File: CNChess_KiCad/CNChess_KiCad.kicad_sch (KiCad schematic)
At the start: 30 parts, among them J1 Servomotor, J2 Barrel_Jack, J3 Motor1, J4 Motor2, J5 Fan, SW1 Limit switch 1, SW2 Limit switch 2, SW3 On/off switch, U1 ESP32C3

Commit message: update kicad schematic
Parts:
- removed C3, C4: 1000uF, symbol Device:C
- removed R3: 10k, symbol Device:R_US
- removed R4: 47k, symbol Device:R_US
- removed TP2: TP3V3, symbol Connector:TestPoint
- added C3, C4: 1000uF, Capacitor_THT:CP_Radial_D8.0mm_P3.50mm, symbol Device:C_Polarized_US
- added D3, D4: LED, Connector_JST:JST_XH_B2B-XH-A_1x02_P2.50mm_Vertical, symbol Device:LED
- added R7: 270, Resistor_THT:R_Axial_DIN0204_L3.6mm_D1.6mm_P5.08mm_Horizontal, symbol Device:R_US
- added R8: 47k, Resistor_THT:R_Axial_DIN0204_L3.6mm_D1.6mm_P5.08mm_Horizontal, symbol Device:R_US
- added U2: Power_Regulator, CNChess_footprints:Reg_12V, symbol CNChess:REG
- C1, C2: footprint (none) -> CNChess_footprints:CAP0_1u
- D1, J5: footprint (none) -> Connector_JST:JST_XH_B2B-XH-A_1x02_P2.50mm_Vertical
- D2: value 5V LED -> 3V3 LED; footprint (none) -> Connector_JST:JST_XH_B2B-XH-A_1x02_P2.50mm_Vertical
- H1, H2: footprint (none) -> MountingHole:MountingHole_3.2mm_M3_Pad
- J1: footprint (none) -> Connector_JST:JST_XH_B3B-XH-A_1x03_P2.50mm_Vertical
- J2: footprint (none) -> CNChess_footprints:BarrelJack_Horizontal
- J3, J4: footprint (none) -> Connector_JST:JST_XH_B4B-XH-A_1x04_P2.50mm_Vertical
- R1: value 660 -> 1000; footprint (none) -> Resistor_THT:R_Axial_DIN0204_L3.6mm_D1.6mm_P5.08mm_Horizontal
- R2: value 200 -> 270; footprint (none) -> Resistor_THT:R_Axial_DIN0204_L3.6mm_D1.6mm_P5.08mm_Horizontal
- R5: value 10k -> 47k; footprint (none) -> Resistor_THT:R_Axial_DIN0204_L3.6mm_D1.6mm_P5.08mm_Horizontal
- R6: value 47k -> 270; footprint (none) -> Resistor_THT:R_Axial_DIN0204_L3.6mm_D1.6mm_P5.08mm_Horizontal
- SW1: value Limit switch 1 -> LSW1; footprint (none) -> Connector_JST:JST_XH_B2B-XH-A_1x02_P2.50mm_Vertical
- SW2: value Limit switch 2 -> LSW2; footprint (none) -> Connector_JST:JST_XH_B2B-XH-A_1x02_P2.50mm_Vertical
- SW3: value On/off switch -> OOSW; footprint (none) -> Connector_JST:JST_XH_B2B-XH-A_1x02_P2.50mm_Vertical
- TMC1, TMC2: value ~ -> Driver; footprint TMC2209_footprint:TMC2209_header -> CNChess_footprints:TMC2209
- TP1: footprint (none) -> TestPoint:TestPoint_Pad_D1.5mm
- TP2: renamed from TP3; footprint (none) -> TestPoint:TestPoint_Pad_D1.5mm
- TP3: renamed from TP4; footprint (none) -> TestPoint:TestPoint_Pad_D1.5mm
- TP4: renamed from TP5; footprint (none) -> TestPoint:TestPoint_Pad_D1.5mm
- U1: footprint TMC2209_footprint:Esp32-C3 -> CNChess_footprints:Esp32-C3
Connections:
- net +12V: now also C3.1, C4.1, U2.1 (EN), U2.2 (IN+); no longer J1.2 (Pin_2)
- net +3V3: now also R2.1, SW1.2, SW2.2; no longer TMC1.10 (VDD), TMC2.10 (VDD)
- net +5V: now also TMC1.10 (VDD), TMC2.10 (VDD); no longer R2.1, R5.1
- net DIR1: now also U1.2 (PA4_A1_D1); no longer U1.5 (PA8_A4_D4_SDA)
- net DIR2: now also U1.4 (PA11_A3_D3); no longer U1.7 (PB08_A6_D6_TX)
- net GND: now also R5.1, C3.2, C4.2, D3.1 (K), D4.1 (K), R8.1, U2.3 (IN-), U2.4 (OUT-); no longer R6.2
- net SERVO: now also U1.7 (PB08_A6_D6_TX); no longer U1.9 (PA7_A8_D8_SCK)
- net STEP1: now also U1.1 (PA02_A0_D0); no longer U1.4 (PA11_A3_D3)
- net STEP2: now also U1.3 (PA10_A2_D2); no longer U1.6 (PA9_A5_D5_SCL)
- net SW1: now also R5.2, R6.2, SW1.1, U1.5 (PA8_A4_D4_SDA); no longer SW1.2, U1.11 (PA6_A10_D10_MOSI)
- net SW2: now also SW2.1, U1.6 (PA9_A5_D5_SCL), R7.2, R8.2; no longer R6.1, SW2.2, U1.10 (PA5_A9_D9_MISO)
- new net: D4.2 (A), R7.1
- new net: D3.2 (A), R6.1
- new net: J1.2 (Pin_2), U2.5 (OUT+)
- no-connect marks 10 -> 14
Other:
- note added: "Limit switches"
- note added: "Power input"
- note added: "Test points"
- note removed: "Limit switches and on/off switch"
- moved on the sheet: C1, D1, D2, H1, H2, J2, J3, J4, J5, R1, R2, SW1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

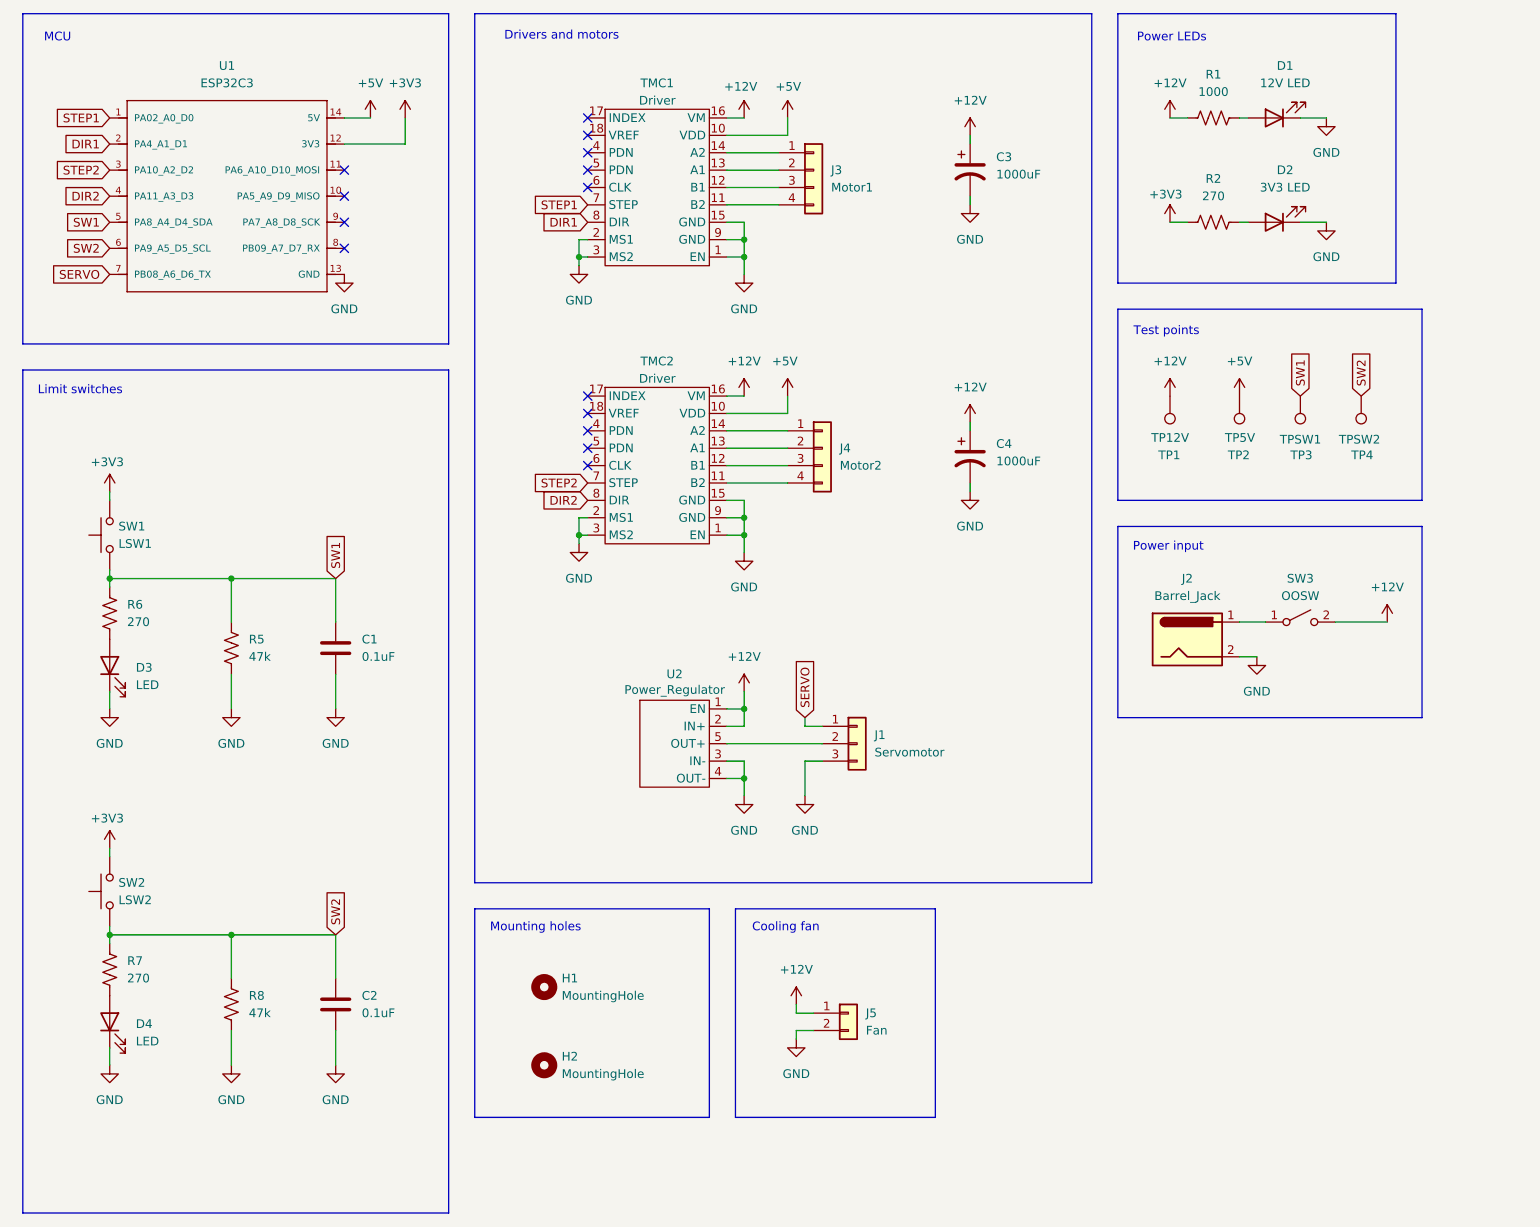
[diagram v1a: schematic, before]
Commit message: PCB tracks + remise tableau de bord 1
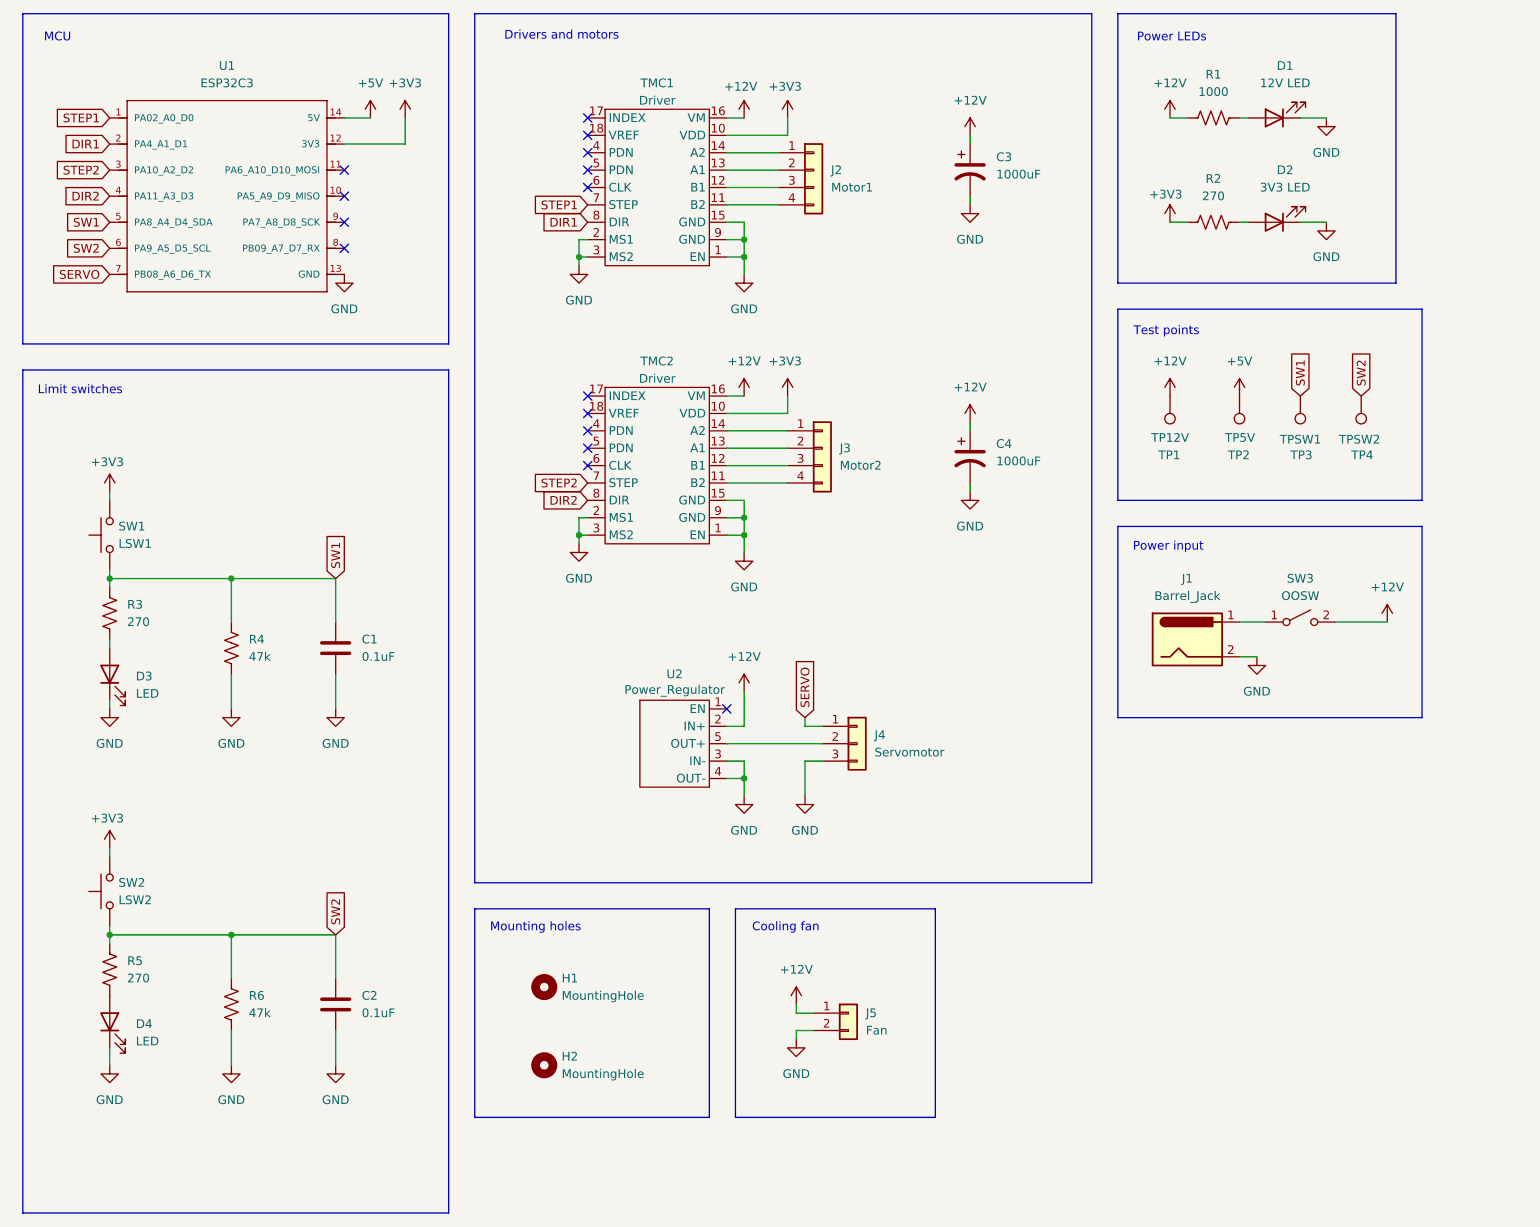
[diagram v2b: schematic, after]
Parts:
- renumbered J2 to J1, J3 to J2, J4 to J3, J1 to J4, R6 to R3, R5 to R4, R7 to R5, R8 to R6
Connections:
- net +12V: no longer U2.1 (EN)
- net +3V3: now also TMC1.10 (VDD), TMC2.10 (VDD)
- net +5V: no longer TMC1.10 (VDD), TMC2.10 (VDD)
- no-connect marks 14 -> 15
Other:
- moved on the sheet: D3
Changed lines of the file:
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@@
 	)
 	(junction
-		(at 121.92 118.11)
-		(diameter 0)
-		(color 0 0 0 0)
-	)
-	(junction
 		(at 121.92 52.07)
 		(diameter 0)
@@
 	)
 	(no_connect
+		(at 119.38 118.11)
+	)
+	(no_connect
 		(at 63.5 50.8)
 	)
@@
 	(wire
 		(pts
-			(xy 121.92 115.57) (xy 121.92 118.11)
+			(xy 121.92 115.57) (xy 121.92 120.65)
 		)
 		(stroke
@@
 	(wire
 		(pts
-			(xy 121.92 120.65) (xy 121.92 118.11)
-		)
-		(stroke
-			(width 0)
-			(type default)
-		)
-	)
-	(wire
-		(pts
 			(xy 119.38 36.83) (xy 127 36.83)
 		)
@@
 	(wire
 		(pts
-			(xy 29.21 115.57) (xy 29.21 118.11)
-		)
-		(stroke
-			(width 0)
-			(type default)
-		)
-	)
-	(wire
-		(pts
 			(xy 46.99 151.13) (xy 62.23 151.13)
 		)
@@
 	(wire
 		(pts
-			(xy 121.92 118.11) (xy 119.38 118.11)
-		)
-		(stroke
-			(width 0)
-			(type default)
-		)
-	)
-	(wire
-		(pts
 			(xy 119.38 31.75) (xy 121.92 31.75)
 		)
@@
 	(wire
 		(pts
+			(xy 29.21 109.22) (xy 29.21 107.95)
+		)
+		(stroke
+			(width 0)
+			(type default)
+		)
+	)
+	(wire
+		(pts
 			(xy 99.06 49.53) (xy 97.79 49.53)
 		)
@@
 	(wire
 		(pts
+			(xy 29.21 116.84) (xy 29.21 118.11)
+		)
+		(stroke
+			(width 0)
+			(type default)
+		)
+	)
+	(wire
+		(pts
 			(xy 29.21 149.86) (xy 29.21 151.13)
 		)
@@
 			)
 		)
-		(property "Value" "+5V"
-			(at 126.492 27.178 0)
+		(property "Value" "+3V3"
+			(at 125.476 27.178 0)
 			(effects
 				(font
@@
 		(dnp no)
 		(fields_autoplaced yes)
-		(property "Reference" "R7"
+		(property "Reference" "R5"
 			(at 31.75 154.9399 0)
 			(effects
@@
 			(project "CNChess_KiCad"
 				(path "/217afebd-c7e0-4ae3-a41a-8884648524ec"
-					(reference "R7")
+					(reference "R5")
 					(unit 1)
 				)
@@
 		(dnp no)
 		(fields_autoplaced yes)
-		(property "Reference" "R6"
+		(property "Reference" "R3"
 			(at 31.75 102.8699 0)
 			(effects
@@
 			(project ""
 				(path "/217afebd-c7e0-4ae3-a41a-8884648524ec"
-					(reference "R6")
+					(reference "R3")
 					(unit 1)
 				)
@@
 		(dnp no)
 		(fields_autoplaced yes)
-		(property "Reference" "J2"
+		(property "Reference" "J1"
 			(at 186.69 99.06 0)
 			(effects
@@
 			(project ""
 				(path "/217afebd-c7e0-4ae3-a41a-8884648524ec"
-					(reference "J2")
+					(reference "J1")
 					(unit 1)
 				)
@@
 		(dnp no)
 		(fields_autoplaced yes)
-		(property "Reference" "R8"
+		(property "Reference" "R6"
 			(at 49.53 160.0199 0)
 			(effects
@@
 			(project "CNChess_KiCad"
 				(path "/217afebd-c7e0-4ae3-a41a-8884648524ec"
-					(reference "R8")
+					(reference "R6")
 					(unit 1)
 				)
@@
 		(dnp no)
 		(fields_autoplaced yes)
-		(property "Reference" "J4"
+		(property "Reference" "J3"
 			(at 135.89 80.0099 0)
 			(effects
@@
 			(project "CNChess_KiCad"
 				(path "/217afebd-c7e0-4ae3-a41a-8884648524ec"
-					(reference "J4")
+					(reference "J3")
 					(unit 1)
 				)
@@
 		(dnp no)
 		(fields_autoplaced yes)
-		(property "Reference" "J1"
+		(property "Reference" "J4"
 			(at 140.97 121.9199 0)
 			(effects
@@
 			(project ""
 				(path "/217afebd-c7e0-4ae3-a41a-8884648524ec"
-					(reference "J1")
+					(reference "J4")
 					(unit 1)
 				)
@@
 		(dnp no)
 		(fields_autoplaced yes)
-		(property "Reference" "J3"
+		(property "Reference" "J2"
 			(at 134.62 39.3699 0)
 			(effects
@@
 			(project ""
 				(path "/217afebd-c7e0-4ae3-a41a-8884648524ec"
-					(reference "J3")
+					(reference "J2")
 					(unit 1)
 				)
@@
 	(symbol
 		(lib_id "Device:LED")
-		(at 29.21 111.76 90)
+		(at 29.21 113.03 90)
 		(unit 1)
 		(exclude_from_sim no)
@@
 		(fields_autoplaced yes)
 		(property "Reference" "D3"
-			(at 33.02 112.0774 90)
+			(at 33.02 113.3474 90)
 			(effects
 				(font
@@
 		)
 		(property "Value" "LED"
-			(at 33.02 114.6174 90)
+			(at 33.02 115.8874 90)
 			(effects
 				(font
@@
 		)
 		(property "Footprint" "Connector_JST:JST_XH_B2B-XH-A_1x02_P2.50mm_Vertical"
-			(at 29.21 111.76 0)
+			(at 29.21 113.03 0)
 			(effects
 				(font
@@
 		)
 		(property "Datasheet" "~"
-			(at 29.21 111.76 0)
+			(at 29.21 113.03 0)
 			(effects
 				(font
@@
 		)
 		(property "Description" "Light emitting diode"
-			(at 29.21 111.76 0)
+			(at 29.21 113.03 0)
 			(effects
 				(font
@@
 		)
 		(property "Sim.Pins" "1=K 2=A"
-			(at 29.21 111.76 0)
+			(at 29.21 113.03 0)
 			(effects
 				(font
@@
 			)
 		)
-		(property "Value" "+5V"
-			(at 125.984 67.31 0)
+		(property "Value" "+3V3"
+			(at 125.476 67.31 0)
 			(effects
 				(font
@@
 		(dnp no)
 		(fields_autoplaced yes)
-		(property "Reference" "R5"
+		(property "Reference" "R4"
 			(at 49.53 107.9499 0)
 			(effects
@@
 			(project ""
 				(path "/217afebd-c7e0-4ae3-a41a-8884648524ec"
-					(reference "R5")
+					(reference "R4")
 					(unit 1)
 				)

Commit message: ajout des modèles 3d et terminé V1 du PCB
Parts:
- C3, C4: footprint Capacitor_THT:CP_Radial_D8.0mm_P3.50mm -> Capacitor_THT:CP_Radial_D10.0mm_P5.00mm
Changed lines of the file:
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@@
 			)
 		)
-		(property "Footprint" "Capacitor_THT:CP_Radial_D8.0mm_P3.50mm"
+		(property "Footprint" "Capacitor_THT:CP_Radial_D10.0mm_P5.00mm"
 			(at 154.94 39.37 0)
 			(effects
@@
 			)
 		)
-		(property "Footprint" "Capacitor_THT:CP_Radial_D8.0mm_P3.50mm"
+		(property "Footprint" "Capacitor_THT:CP_Radial_D10.0mm_P5.00mm"
 			(at 154.94 81.28 0)
 			(effects
